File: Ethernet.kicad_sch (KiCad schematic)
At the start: 0 parts

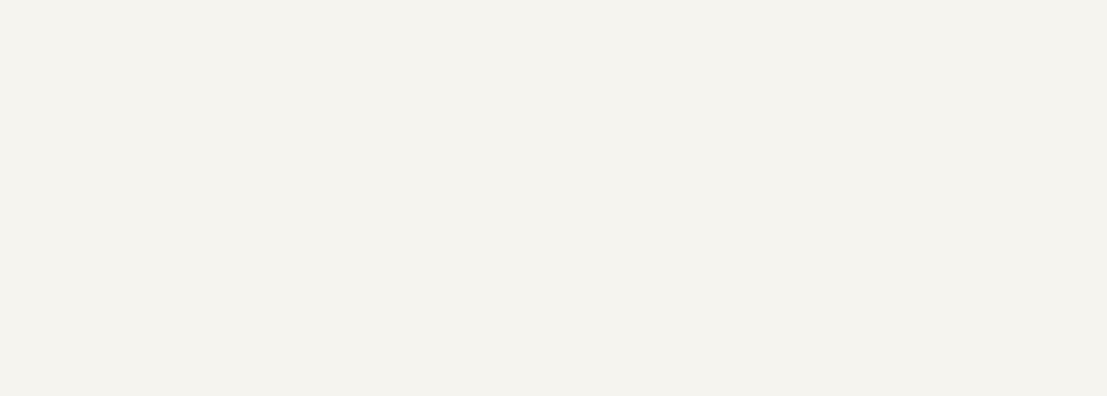
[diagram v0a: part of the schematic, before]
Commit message: Use local labels for RGB bus in folio and add title for all folio
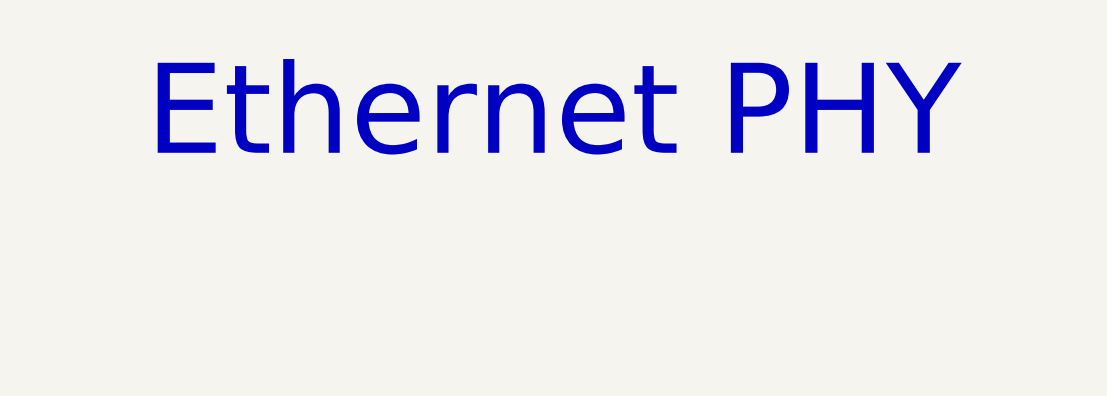
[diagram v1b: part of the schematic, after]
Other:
- note added: "Ethernet PHY"
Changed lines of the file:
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@@
 	(generator_version "9.0")
 	(paper "A4")
+	(text "Ethernet PHY"
+		(exclude_from_sim no)
+		(at 145.288 23.114 0)
+		(effects
+			(font
+				(size 10 10)
+			)
+		)
+	)
 	(hierarchical_label "MOSI_Ethernet"
 		(shape input)

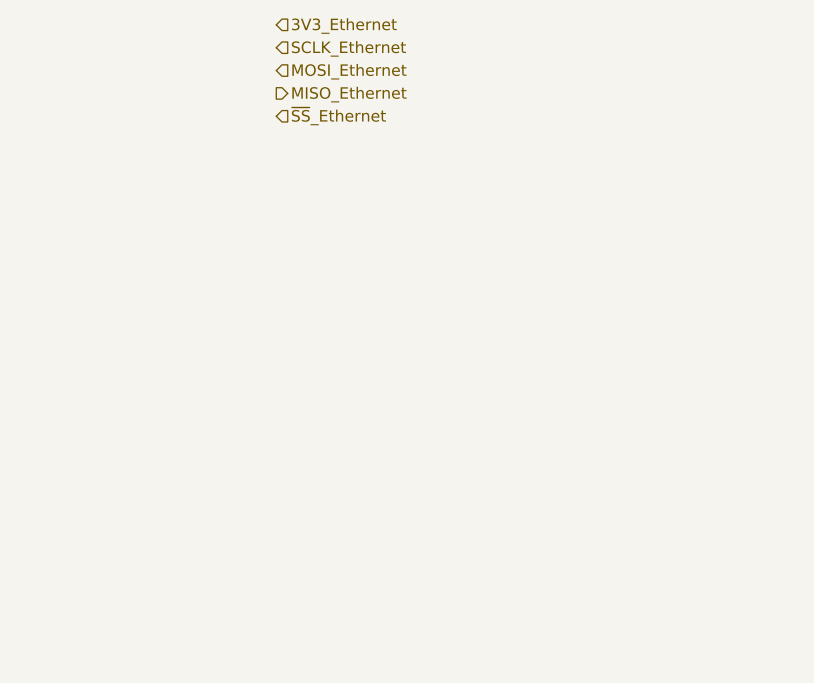
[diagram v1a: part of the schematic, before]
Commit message: Add external Ethernet PHY in SPI (limited to 10 Mbits/s)
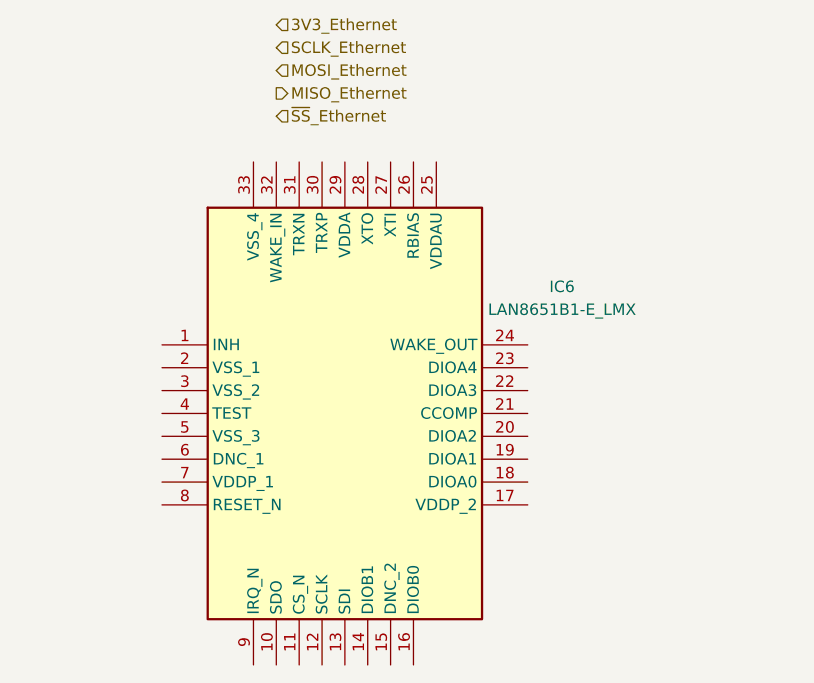
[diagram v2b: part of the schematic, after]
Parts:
- added IC6: LAN8651B1-E_LMX, QFN50P500X500X100-33N-D, symbol weather-station-poc-sym:LAN8651B1-E_LMX
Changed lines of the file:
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@@
+		)
+	)
+	(symbol
+		(lib_id "weather-station-poc-sym:LAN8651B1-E_LMX")
+		(at 123.19 111.76 0)
+		(unit 1)
+		(exclude_from_sim no)
+		(in_bom yes)
+		(on_board yes)
+		(dnp no)
+		(fields_autoplaced yes)
+		(property "Reference" "IC6"
+			(at 167.64 105.3045 0)
+			(effects
+				(font
+					(size 1.27 1.27)
+				)
+			)
+		)
+		(property "Value" "LAN8651B1-E_LMX"
+			(at 167.64 107.8445 0)
+			(effects
+				(font
+					(size 1.27 1.27)
+				)
+			)
+		)
+		(property "Footprint" "QFN50P500X500X100-33N-D"
+			(at 160.02 193.98 0)
+			(effects
+				(font
+					(size 1.27 1.27)
+				)
+				(justify left top)
+				(hide yes)
+			)
+		)
+		(property "Datasheet" "https://ww1.microchip.com/downloads/aemDocuments/documents/AIS/ProductDocuments/DataSheets/LAN8650-1-Data-Sheet-60001734.pdf"
+			(at 160.02 293.98 0)
+			(effects
+				(font
+					(size 1.27 1.27)
+				)
+				(justify left top)
+				(hide yes)
+			)
+		)
+		(property "Description" "Ethernet ICs 10BASE-T1S MAC-PHY with SPI"
+			(at 123.19 111.76 0)
+			(effects
+				(font
+					(size 1.27 1.27)
+				)
+				(hide yes)
+			)
+		)
+		(property "Height" "1"
+			(at 160.02 493.98 0)
+			(effects
+				(font
+					(size 1.27 1.27)
+				)
+				(justify left top)
+				(hide yes)
+			)
+		)
+		(property "Mouser Part Number" "579-LAN8651B1-E/LMX"
+			(at 160.02 593.98 0)
+			(effects
+				(font
+					(size 1.27 1.27)
+				)
+				(justify left top)
+				(hide yes)
+			)
+		)
+		(property "Mouser Price/Stock" "https://www.mouser.co.uk/ProductDetail/Microchip-Technology/LAN8651B1-E-LMX?qs=HoCaDK9Nz5cTGz8XEJbodA%3D%3D"
+			(at 160.02 693.98 0)
+			(effects
+				(font
+					(size 1.27 1.27)
+				)
+				(justify left top)
+				(hide yes)
+			)
+		)
+		(property "Manufacturer_Name" "Microchip"
+			(at 160.02 793.98 0)
+			(effects
+				(font
+					(size 1.27 1.27)
+				)
+				(justify left top)
+				(hide yes)
+			)
+		)
+		(property "Manufacturer_Part_Number" "LAN8651B1-E/LMX"
+			(at 160.02 893.98 0)
+			(effects
+				(font
+					(size 1.27 1.27)
+				)
+				(justify left top)
+				(hide yes)
+			)
+		)
+		(pin "28"
+		)
+		(pin "15"
+		)
+		(pin "24"
+		)
+		(pin "14"
+		)
+		(pin "19"
+		)
+		(pin "17"
+		)
+		(pin "21"
+		)
+		(pin "7"
+		)
+		(pin "11"
+		)
+		(pin "8"
+		)
+		(pin "3"
+		)
+		(pin "32"
+		)
+		(pin "30"
+		)
+		(pin "12"
+		)
+		(pin "29"
+		)
+		(pin "26"
+		)
+		(pin "16"
+		)
+		(pin "5"
+		)
+		(pin "25"
+		)
+		(pin "1"
+		)
+		(pin "6"
+		)
+		(pin "9"
+		)
+		(pin "4"
+		)
+		(pin "10"
+		)
+		(pin "2"
+		)
+		(pin "33"
+		)
+		(pin "31"
+		)
+		(pin "13"
+		)
+		(pin "27"
+		)
+		(pin "23"
+		)
+		(pin "22"
+		)
+		(pin "20"
+		)
+		(pin "18"
+		)
+		(instances
+			(project ""
+				(path "/38eb53bb-294e-46e4-ad59-fd355ca373b9/dba7376c-12da-4b87-819b-9e31ed4c088a"
+					(reference "IC6")
+					(unit 1)
+				)
+			)
 		)
 	)

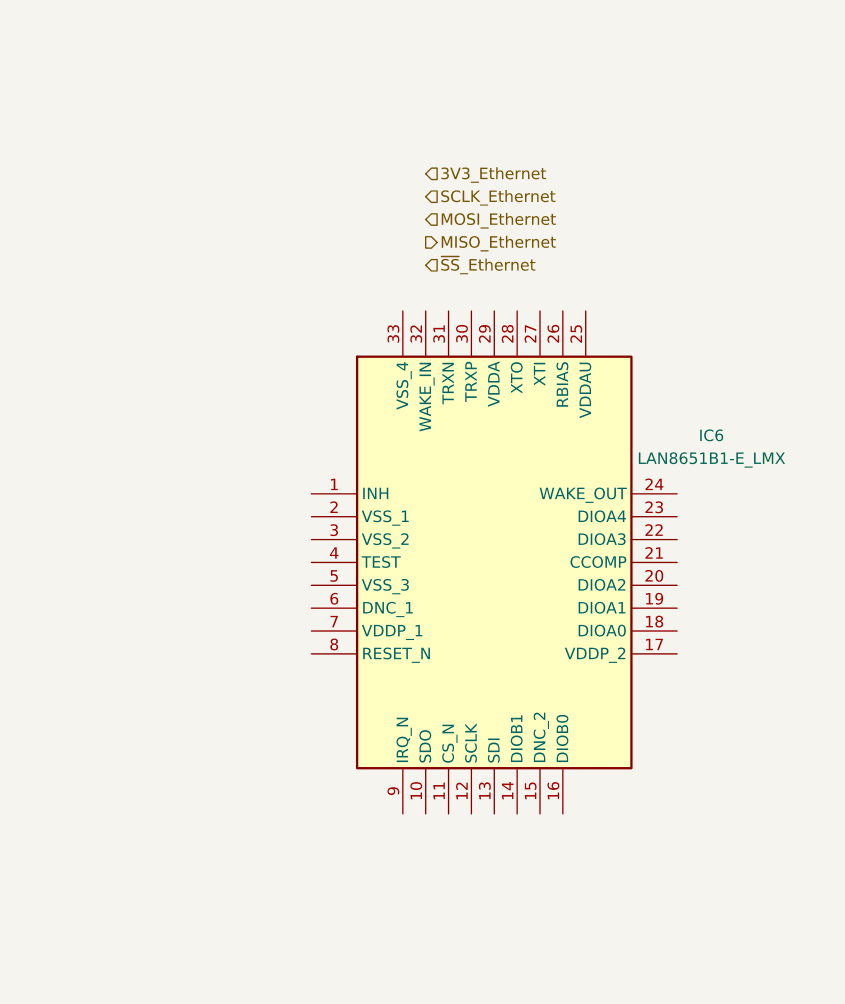
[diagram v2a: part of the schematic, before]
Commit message: Fix some ERC errors
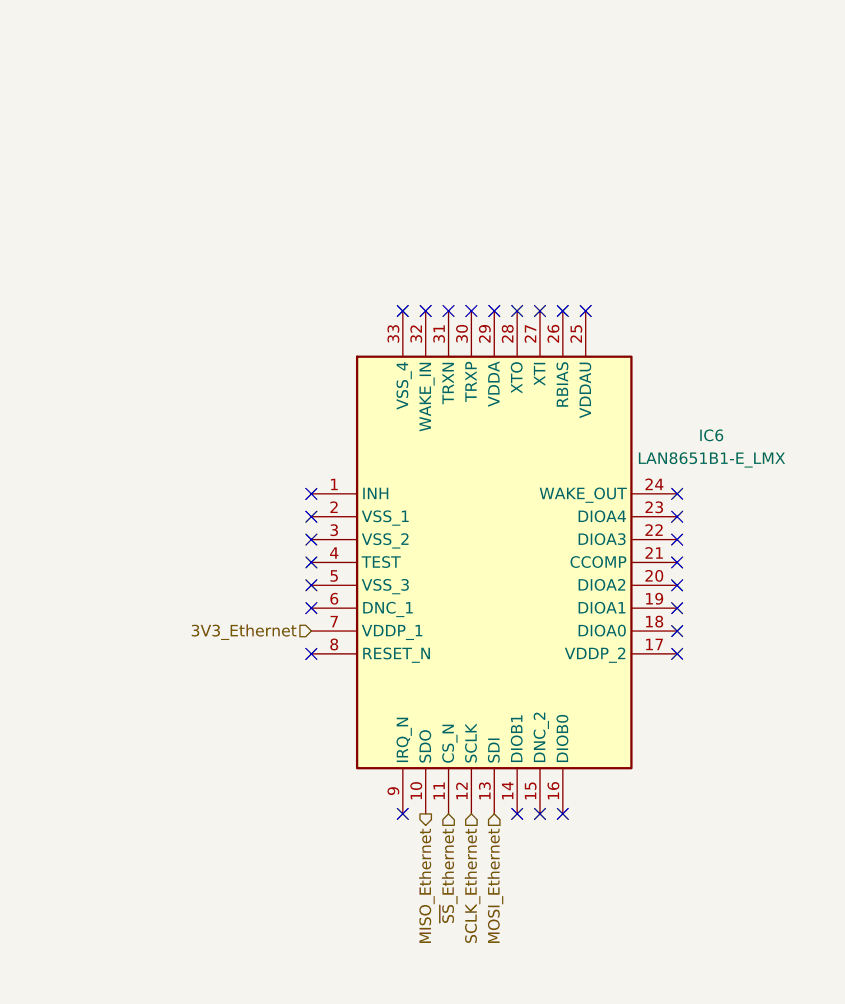
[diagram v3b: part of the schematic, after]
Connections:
- net 3V3_Ethernet: now also IC6.7 (VDDP_1)
- net MISO_Ethernet: now also IC6.10 (SDO)
- net MOSI_Ethernet: now also IC6.13 (SDI)
- net SCLK_Ethernet: now also IC6.12 (SCLK)
- net ~{SS}_Ethernet: now also IC6.11 (CS_N)
- no-connect marks 0 -> 28
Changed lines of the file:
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@@
 		)
+	)
+	(no_connect
+		(at 163.83 129.54)
+	)
+	(no_connect
+		(at 123.19 121.92)
+	)
+	(no_connect
+		(at 148.59 147.32)
+	)
+	(no_connect
+		(at 133.35 91.44)
+	)
+	(no_connect
+		(at 163.83 114.3)
+	)
+	(no_connect
+		(at 151.13 147.32)
+	)
+	(no_connect
+		(at 163.83 116.84)
+	)
+	(no_connect
+		(at 133.35 147.32)
+	)
+	(no_connect
+		(at 163.83 124.46)
+	)
+	(no_connect
+		(at 123.19 114.3)
+	)
+	(no_connect
+		(at 151.13 91.44)
+	)
+	(no_connect
+		(at 148.59 91.44)
+	)
+	(no_connect
+		(at 153.67 91.44)
+	)
+	(no_connect
+		(at 146.05 147.32)
+	)
+	(no_connect
+		(at 123.19 111.76)
+	)
+	(no_connect
+		(at 140.97 91.44)
+	)
+	(no_connect
+		(at 138.43 91.44)
+	)
+	(no_connect
+		(at 123.19 116.84)
+	)
+	(no_connect
+		(at 163.83 111.76)
+	)
+	(no_connect
+		(at 163.83 121.92)
+	)
+	(no_connect
+		(at 123.19 124.46)
+	)
+	(no_connect
+		(at 143.51 91.44)
+	)
+	(no_connect
+		(at 123.19 129.54)
+	)
+	(no_connect
+		(at 123.19 119.38)
+	)
+	(no_connect
+		(at 135.89 91.44)
+	)
+	(no_connect
+		(at 163.83 127)
+	)
+	(no_connect
+		(at 146.05 91.44)
+	)
+	(no_connect
+		(at 163.83 119.38)
 	)
 	(hierarchical_label "MOSI_Ethernet"
 		(shape input)
-		(at 135.89 81.28 0)
+		(at 143.51 147.32 270)
 		(effects
 			(font
 				(size 1.27 1.27)
 			)
-			(justify left)
+			(justify right)
 		)
 	)
 	(hierarchical_label "~{SS}_Ethernet"
 		(shape input)
-		(at 135.89 86.36 0)
+		(at 138.43 147.32 270)
 		(effects
 			(font
 				(size 1.27 1.27)
 			)
-			(justify left)
+			(justify right)
 		)
 	)
 	(hierarchical_label "MISO_Ethernet"
 		(shape output)
-		(at 135.89 83.82 0)
+		(at 135.89 147.32 270)
 		(effects
 			(font
 				(size 1.27 1.27)
 			)
-			(justify left)
+			(justify right)
 		)
 	)
 	(hierarchical_label "SCLK_Ethernet"
 		(shape input)
-		(at 135.89 78.74 0)
+		(at 140.97 147.32 270)
 		(effects
 			(font
 				(size 1.27 1.27)
 			)
-			(justify left)
+			(justify right)
 		)
 	)
 	(hierarchical_label "3V3_Ethernet"
 		(shape input)
-		(at 135.89 76.2 0)
+		(at 123.19 127 180)
 		(effects
 			(font
 				(size 1.27 1.27)
 			)
-			(justify left)
+			(justify right)
 		)
 	)

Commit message: Fix warnings for footprint
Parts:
- IC6: footprint QFN50P500X500X100-33N-D -> weather-station-poc-fp:QFN50P500X500X100-33N-D
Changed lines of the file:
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@@
 			)
 		)
-		(property "Footprint" "QFN50P500X500X100-33N-D"
+		(property "Footprint" "weather-station-poc-fp:QFN50P500X500X100-33N-D"
 			(at 160.02 193.98 0)
 			(effects
